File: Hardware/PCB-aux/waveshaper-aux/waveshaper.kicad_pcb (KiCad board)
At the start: 2 copper layers, 189 x 174 mm, 63 parts, among them J1 2x7 IDC header, J10 AudioJack2_SwitchT, J11 2_pin_Molex_header, J12 AudioJack2_SwitchT, J13 3_pin_Molex_header, J14 2x5 pin socket, J15 AudioJack2_SwitchT, J16 AudioJack2_SwitchT, J17 AudioJack2_SwitchT, J18 AudioJack2_SwitchT, J3 AudioJack2_SwitchT, J4 AudioJack2_SwitchT, J5 2_pin_Molex_header, J6 EURO_PWR_2x5, J7 AudioJack2_SwitchT, J8 Conn_01x9, J9 Conn_01x9, SW1 SW_SPDT, U1 4066, U2 4066, U3 MCP6004, U4 MCP6004, U5 LM4040DIZ-10

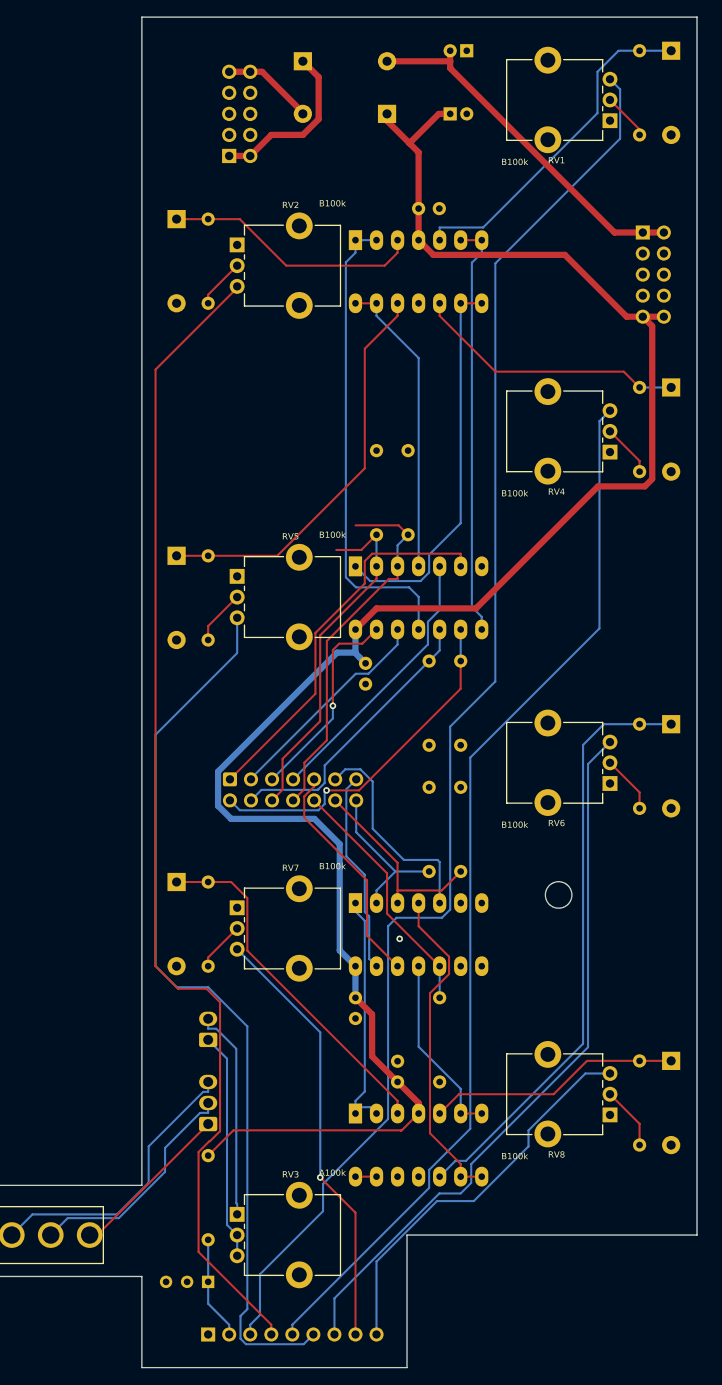
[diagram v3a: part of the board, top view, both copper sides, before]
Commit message: rm op amp, reroute
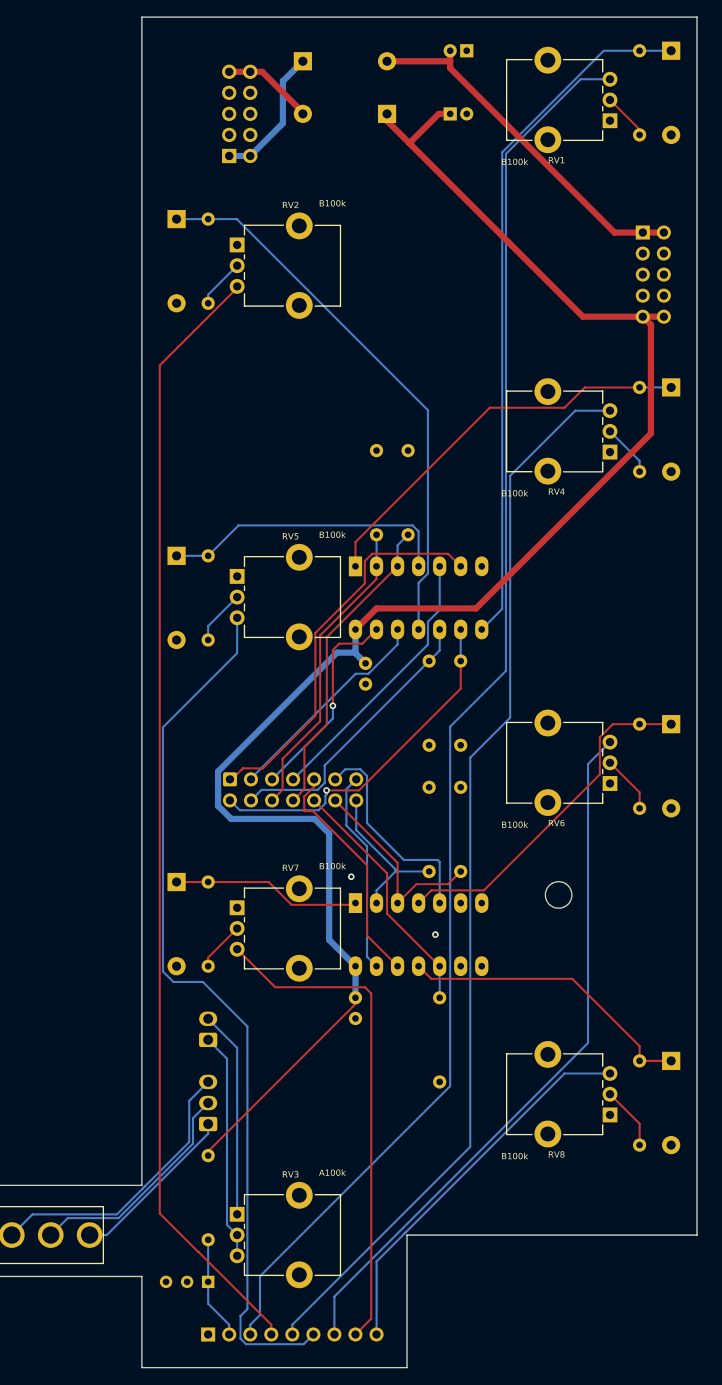
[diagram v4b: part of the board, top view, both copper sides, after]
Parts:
- removed C1, C2: 100nF, ao_tht:C_Disc_D3.0mm_W1.6mm_P2.50mm
- removed U3, U4: MCP6004, ao_tht:DIP-14_W7.62mm_Socket_LongPads
- R1, R2, R3, R4, R5, R6, R7: value 100k -> 1M
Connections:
- D3 pad 1: P_+3 -> CV_+3
- D4 pad 1: P_+2 -> CV_+2
- D5 pad 1: P_+1 -> CV_+1
- D6 pad 1: P_0 -> CV_0
- D7 pad 1: P_-1 -> CV_-1
- D8 pad 1: P_-2 -> CV_-2
- D9 pad 1: P_-3 -> CV_-3
- R10 pad 2: P_+2 -> CV_+2
- R11 pad 2: P_+1 -> CV_+1
- R12 pad 2: P_0 -> CV_0
- R13 pad 2: P_-1 -> CV_-1
- R14 pad 2: P_-2 -> CV_-2
- R15 pad 2: P_-3 -> CV_-3
- R9 pad 2: P_+3 -> CV_+3
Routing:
- net P_-1: track 71.7 -> 0.00 mm
- net P_0: track 48.6 -> 0.00 mm
- net P_-2: track 42.8 -> 0.00 mm
- net P_+3: track 41.2 -> 0.00 mm
- net CV_+3: track 50.5 -> 84.1 mm
- net P_+1: track 33.0 -> 0.00 mm
- net P_+2: track 31.2 -> 0.00 mm
- net P_-3: track 30.6 -> 0.00 mm
- net +12V: track 232.2 -> 204.0 mm
- net CV_-3: track 22.4 -> 36.3 mm
- net CV_+2: track 57.4 -> 66.8 mm
- net Net-(J9-Pad8): track 52.4 -> 60.3 mm, vias 1 -> 0
- net MIXIN_0: track 45.2 -> 37.8 mm
- net CV_-2: track 29.2 -> 22.8 mm
- net MIXIN_+1: track 42.9 -> 37.3 mm
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
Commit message: Trace tweaks, Gerbers
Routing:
- net Net-(J9-Pad5): track 129.8 -> 132.8 mm
- net /Panel and power/SL_HIGH: track 34.3 -> 36.3 mm
- net /Panel and power/SL_MED: track 20.5 -> 22.5 mm
- net /Panel and power/SLEW: track 27.4 -> 29.4 mm
- net Net-(J9-Pad9): track 46.4 -> 47.9 mm
- net Net-(J9-Pad7): track 85.3 -> 86.3 mm

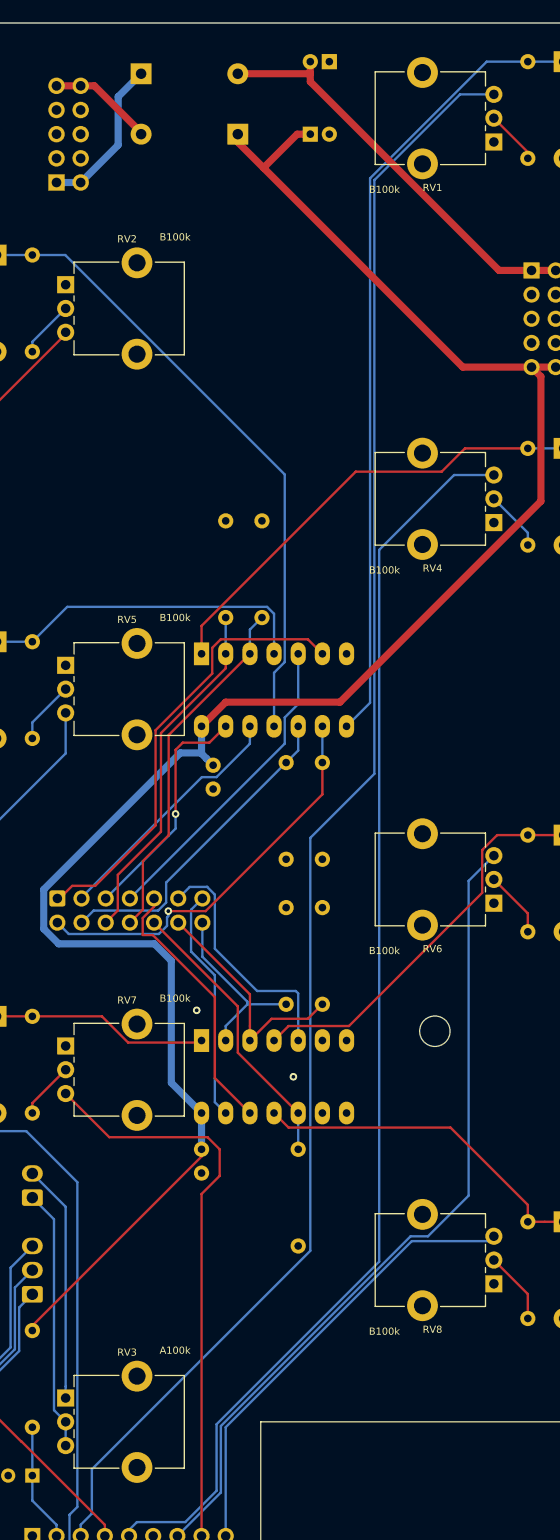
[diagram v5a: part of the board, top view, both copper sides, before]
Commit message: Change pot footprint, new Gerbers
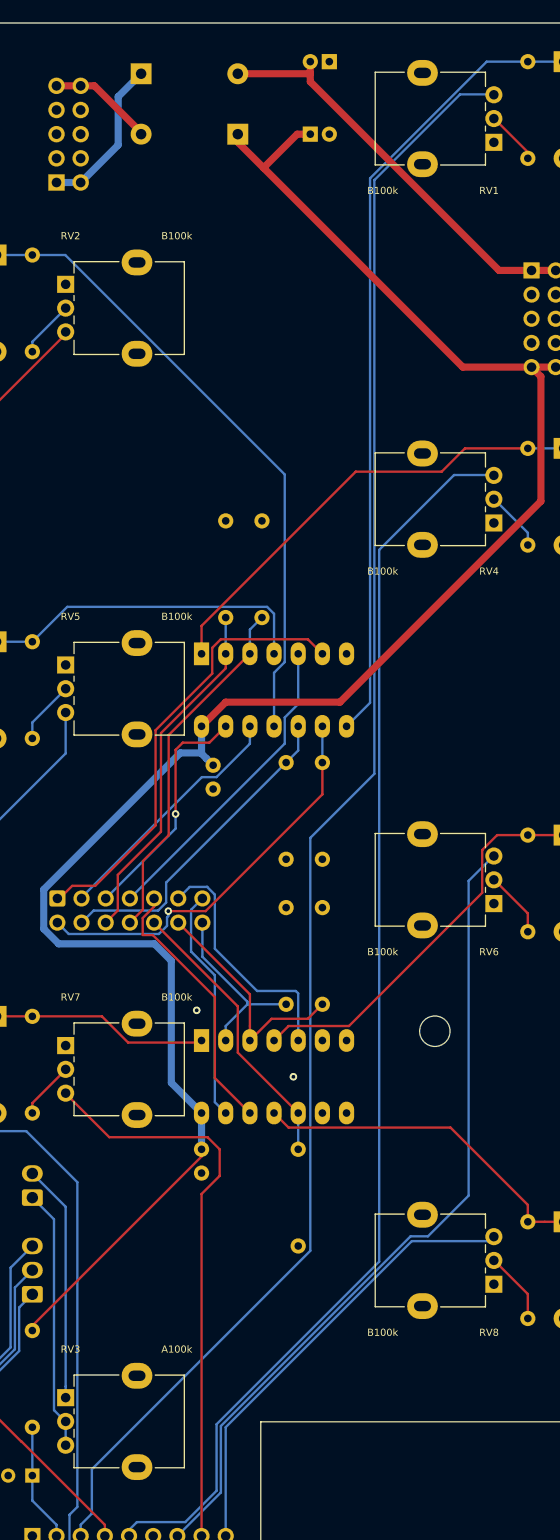
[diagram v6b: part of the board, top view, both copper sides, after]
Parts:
- added GRAF2: Holes, waveshaper:waveshaper-holes, F.Cu at (131.0, 106.0)
- RV1, RV2, RV3, RV4, RV5, RV6, RV7, RV8: footprint ao_tht:Potentiometer_Alpha_RD901F-40-00D_Single_Vertical_CircularHoles_centered -> ao_tht:Potentiometer_Alpha_RD901F-40-00D_Single_Vertical
- moved RV4 7.92 mm to (168.5, 71.5)
- moved RV5 7.92 mm to (123.5, 86.5)
- moved RV6 7.92 mm to (168.5, 111.5)
- moved RV7 7.92 mm to (123.5, 126.5)
- moved RV1 7.92 mm to (168.5, 31.5)
- moved RV2 7.92 mm to (123.5, 46.5)
- moved RV3 7.92 mm to (123.5, 163.5)
- moved RV8 7.92 mm to (168.5, 151.5)
